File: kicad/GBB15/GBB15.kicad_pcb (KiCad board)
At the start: 4 copper layers, 67 x 15 mm, 74 parts, among them J1 CAN_IN, J10 USB-C, J2 CAN_OUT, J3 MA_THERM, J4 MB_THERM, J5 MA, J6 MB, J7 ENDSTOP1, J8 ENDSTOP2, SW1 BOOT, SW2 RESET, U1 TMC2209-LA-T, U2 STM32G0B1CEU6, U3 TMC2209-LA-T, U4 MAX3051EKA+T, U5 NCP730BMT330TBG, Y1 Crystal_GND24

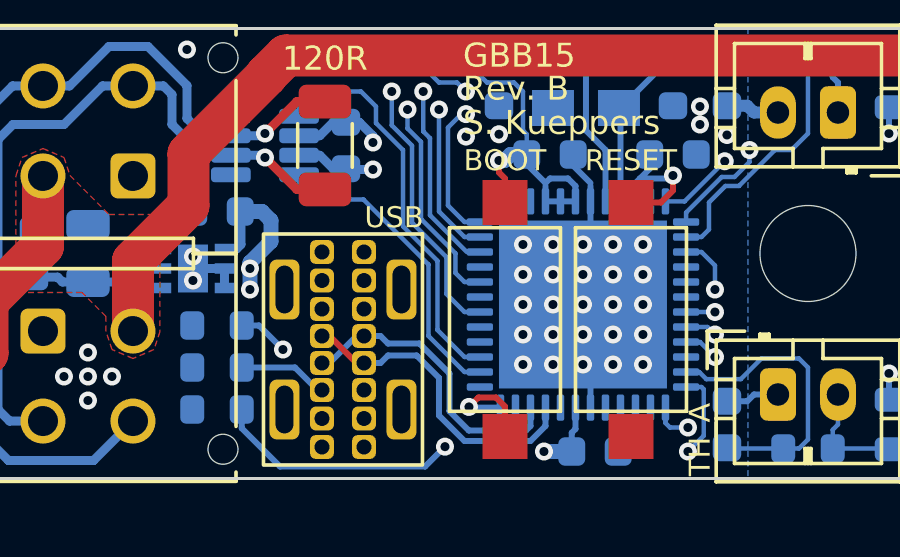
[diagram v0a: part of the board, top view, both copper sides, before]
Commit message: Added additional debug pads for SWD
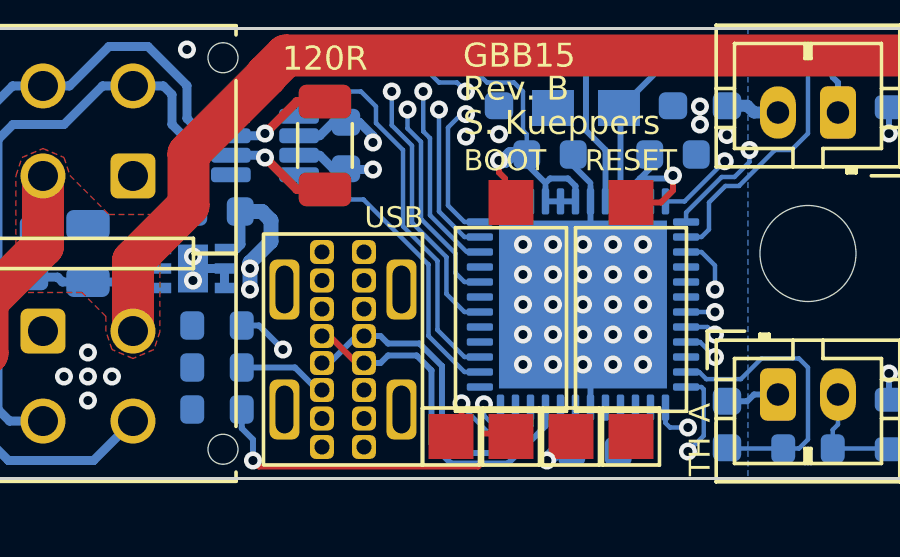
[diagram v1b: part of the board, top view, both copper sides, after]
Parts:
- added TP1: TestPoint, TestPoint:TestPoint_Pad_1.5x1.5mm, F.Cu at (153.6, 98.1)
- added TP2: TestPoint, TestPoint:TestPoint_Pad_1.5x1.5mm, F.Cu at (149.6, 98.1)
- moved SW1 0.20 mm to (151.6, 94.2)
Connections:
- U2 pad 35: unconnected-(U2-Pad35) -> /SWDIO
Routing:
- net /SWDIO: track 0.00 -> 4.25 mm, vias 0 -> 1
- net /USB_DP: track 10.0 -> 11.4 mm
- net /USB_DM: track 10.7 -> 12.0 mm
- net /BOOT0: track 13.2 -> 14.0 mm
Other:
- board text added: "+3V3"
- board text added: "SWCLK"
- board text added: "SWD"
- board text added: "SWDIO"

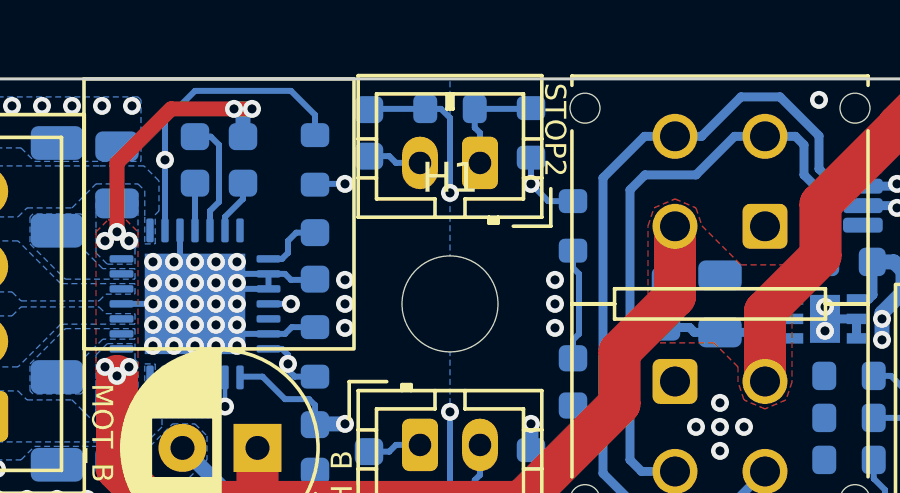
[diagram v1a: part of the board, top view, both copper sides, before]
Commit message: Increased connection width to MicroFit GND pads
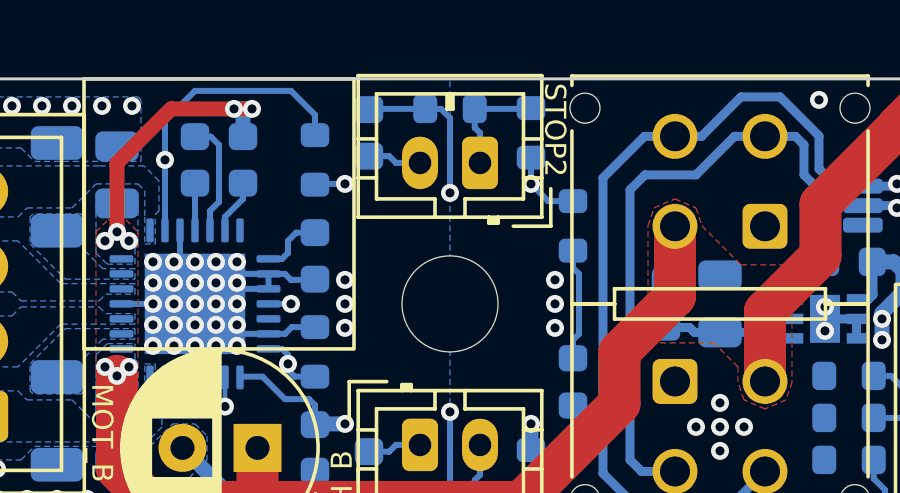
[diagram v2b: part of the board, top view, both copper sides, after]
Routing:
- net GND: track 80.4 -> 90.1 mm
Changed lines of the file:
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@@
     (property "Sheetname" "")
     (attr exclude_from_pos_files)
-    (fp_text reference "H1" (at 0 -4.2) (layer "F.SilkS")
+    (fp_text reference "H1" (at 0 -4.2) (layer "F.SilkS") hide
       (effects (font (size 1 1) (thickness 0.15)))
     )
@@
       (effects (font (size 1 1) (thickness 0.15)))
     )
-    (fp_text value "RESET" (at 4.3 0.3 180) (layer "F.Fab")
+    (fp_text value "RESET" (at 6.5 0.4 180) (layer "F.Fab")
       (effects (font (size 1 1) (thickness 0.15)))
     )
@@
       (effects (font (size 1 1) (thickness 0.15)))
     )
-    (fp_text user "${REFERENCE}" (at 0 -1.65) (layer "F.Fab")
+    (fp_text user "${REFERENCE}" (at 0 -1.65) (layer "F.Fab") hide
       (effects (font (size 1 1) (thickness 0.15)))
     )
@@
       (effects (font (size 1 1) (thickness 0.15)))
     )
-    (fp_text value "USB-C" (at 5.5 0 unlocked) (layer "F.Fab")
+    (fp_text value "USB-C" (at 5.5 0.2 unlocked) (layer "F.Fab")
       (effects (font (size 1 1) (thickness 0.15)))
     )
@@
       (effects (font (size 1 1) (thickness 0.15)))
     )
-    (fp_text user "${REFERENCE}" (at 0 -1.65) (layer "F.Fab")
+    (fp_text user "${REFERENCE}" (at 0 -1.65) (layer "F.Fab") hide
       (effects (font (size 1 1) (thickness 0.15)))
     )
@@
       (effects (font (size 1 1) (thickness 0.15)))
     )
-    (fp_text value "BOOT" (at -4.3 -0.5) (layer "F.Fab")
+    (fp_text value "BOOT" (at -6.5 -0.8) (layer "F.Fab")
       (effects (font (size 1 1) (thickness 0.15)))
     )
@@
       (effects (font (size 1 1) (thickness 0.15)))
     )
-    (fp_text value "MA_THERM" (at 1 4) (layer "F.Fab")
+    (fp_text value "MA_THERM" (at 1.2 4) (layer "F.Fab")
       (effects (font (size 1 1) (thickness 0.15)))
     )
@@
     (fp_line (start 0.8 0.735) (end -1.485 0.735) (layer "B.SilkS") (width 0.12))
     (fp_line (start 1.48 0.73) (end 1.48 -0.73) (layer "B.CrtYd") (width 0.05))
+    (fp_line (start 1.48 -0.73) (end -1.48 -0.73) (layer "B.CrtYd") (width 0.05))
     (fp_line (start -1.48 0.73) (end 1.48 0.73) (layer "B.CrtYd") (width 0.05))
     (fp_line (start -1.48 -0.73) (end -1.48 0.73) (layer "B.CrtYd") (width 0.05))
-    (fp_line (start 1.48 -0.73) (end -1.48 -0.73) (layer "B.CrtYd") (width 0.05))
-    (fp_line (start 0.8 -0.4) (end 0.8 0.4) (layer "B.Fab") (width 0.1))
     (fp_line (start 0.8 0.4) (end -0.5 0.4) (layer "B.Fab") (width 0.1))
-    (fp_line (start -0.8 0.1) (end -0.8 -0.4) (layer "B.Fab") (width 0.1))
     (fp_line (start -0.8 -0.4) (end 0.8 -0.4) (layer "B.Fab") (width 0.1))
     (fp_line (start -0.5 0.4) (end -0.8 0.1) (layer "B.Fab") (width 0.1))
+    (fp_line (start -0.8 0.1) (end -0.8 -0.4) (layer "B.Fab") (width 0.1))
+    (fp_line (start 0.8 -0.4) (end 0.8 0.4) (layer "B.Fab") (width 0.1))
     (pad "1" smd roundrect (at -0.7875 0 90) (size 0.875 0.95) (layers "B.Cu" "B.Paste" "B.Mask") (roundrect_rratio 0.25)
       (net 15 "GND") (pinfunction "K") (pintype "passive"))
@@
   (gr_line (start 137.5 103) (end 137.5 110) (layer "Dwgs.User") (width 0.15))
   (gr_line (start 107 87) (end 101 87) (layer "Dwgs.User") (width 0.15))
-  (gr_line (start 152.6 103) (end 152.6 109) (layer "Dwgs.User") (width 0.15))
+  (gr_line (start 152.6 104) (end 152.6 110) (layer "Dwgs.User") (width 0.15))
   (gr_line (start 183 97) (end 189 97) (layer "Dwgs.User") (width 0.15))
   (gr_line (start 101 87) (end 101 97) (layer "Dwgs.User") (width 0.15))
   (gr_line (start 101 89.5) (end 107 89.5) (layer "Dwgs.User") (width 0.15))
-  (gr_rect (start 148.4 103) (end 156.7 109) (layer "Dwgs.User") (width 0.15) (fill none))
+  (gr_rect (start 148.4 104) (end 156.7 110) (layer "Dwgs.User") (width 0.15) (fill none))
   (gr_line (start 189 89.5) (end 189 87) (layer "Dwgs.User") (width 0.15))
   (gr_line (start 107 89.5) (end 107 87) (layer "Dwgs.User") (width 0.15))
@@
   (gr_line (start 189 87) (end 183 87) (layer "Dwgs.User") (width 0.15))
   (gr_line (start 189 92) (end 183 92) (layer "Dwgs.User") (width 0.15))
-  (gr_line (start 150.5 103) (end 150.5 109) (layer "Dwgs.User") (width 0.15))
+  (gr_line (start 150.5 104) (end 150.5 110) (layer "Dwgs.User") (width 0.15))
   (gr_line (start 189 97) (end 189 89.5) (layer "Dwgs.User") (width 0.15))
   (gr_line (start 189 94.5) (end 183 94.5) (layer "Dwgs.User") (width 0.15))
@@
   (gr_line (start 107 97) (end 107 89.5) (layer "Dwgs.User") (width 0.15))
   (gr_line (start 137.5 74) (end 137.5 81) (layer "Dwgs.User") (width 0.15))
-  (gr_line (start 154.7 103) (end 154.7 109) (layer "Dwgs.User") (width 0.15))
+  (gr_line (start 154.7 104) (end 154.7 110) (layer "Dwgs.User") (width 0.15))
   (gr_line (start 183 89.5) (end 189 89.5) (layer "Dwgs.User") (width 0.15))
   (gr_line (start 107 94.5) (end 101 94.5) (layer "Dwgs.User") (width 0.15))
@@
     (effects (font (size 1 1) (thickness 0.15)))
   )
-  (gr_text "SWCLK\n" (at 151.6 105.7 90) (layer "Dwgs.User")
+  (gr_text "SWCLK\n" (at 151.6 106.7 90) (layer "Dwgs.User")
     (effects (font (size 1 1) (thickness 0.15)))
   )
@@
     (effects (font (size 1 1) (thickness 0.15)))
   )
-  (gr_text "+3V3" (at 153.7 105.7 90) (layer "Dwgs.User")
+  (gr_text "+3V3" (at 153.7 106.7 90) (layer "Dwgs.User")
     (effects (font (size 1 1) (thickness 0.15)))
   )
@@
     (effects (font (size 1 1) (thickness 0.15)))
   )
-  (gr_text "SWD" (at 152.5 100.7) (layer "Dwgs.User")
+  (gr_text "SWD" (at 152.6 103.2) (layer "Dwgs.User")
     (effects (font (size 1 1) (thickness 0.15)))
   )
@@
     (effects (font (size 1 1) (thickness 0.15)))
   )
-  (gr_text "SWDIO\n" (at 149.5 105.7 90) (layer "Dwgs.User")
+  (gr_text "SWDIO\n" (at 149.5 106.7 90) (layer "Dwgs.User")
     (effects (font (size 1 1) (thickness 0.15)))
   )
@@
     (effects (font (size 1 1) (thickness 0.15)))
   )
-  (gr_text "GND" (at 155.8 105.7 90) (layer "Dwgs.User")
+  (gr_text "GND" (at 155.8 106.7 90) (layer "Dwgs.User")
     (effects (font (size 1 1) (thickness 0.15)))
   )
@@
   (via (at 132 91.2) (size 0.6) (drill 0.3) (layers "F.Cu" "B.Cu") (net 15))
   (via (at 118.6 90.6) (size 0.6) (drill 0.3) (layers "F.Cu" "B.Cu") (net 15))
+  (segment (start 139 89.4) (end 137.785 89.4) (width 0.8) (layer "In1.Cu") (net 15))
+  (segment (start 139 89.4) (end 140.215 89.4) (width 0.8) (layer "In1.Cu") (net 15))
   (segment (start 145.3 98.45) (end 146.05 98.45) (width 0.2) (layer "In1.Cu") (net 15))
+  (segment (start 139 89.4) (end 139 90.615) (width 0.8) (layer "In1.Cu") (net 15))
+  (segment (start 139 89.415) (end 139 88.2) (width 0.8) (layer "In1.Cu") (net 15))
+  (segment (start 136 94.6) (end 136 95.815) (width 0.8) (layer "In1.Cu") (net 15))
+  (segment (start 136 94.6) (end 137.215 94.6) (width 0.8) (layer "In1.Cu") (net 15))
+  (segment (start 136 94.6) (end 134.785 94.6) (width 0.8) (layer "In1.Cu") (net 15))
   (segment (start 146 92) (end 146.05 91.95) (width 0.2) (layer "In1.Cu") (net 15))
+  (segment (start 136 94.615) (end 136 93.4) (width 0.8) (layer "In1.Cu") (net 15))
   (segment (start 146 98.4) (end 146 92) (width 0.2) (layer "In1.Cu") (net 15))
   (segment (start 146.05 98.45) (end 146.7 98.45) (width 0.2) (layer "In1.Cu") (net 15))

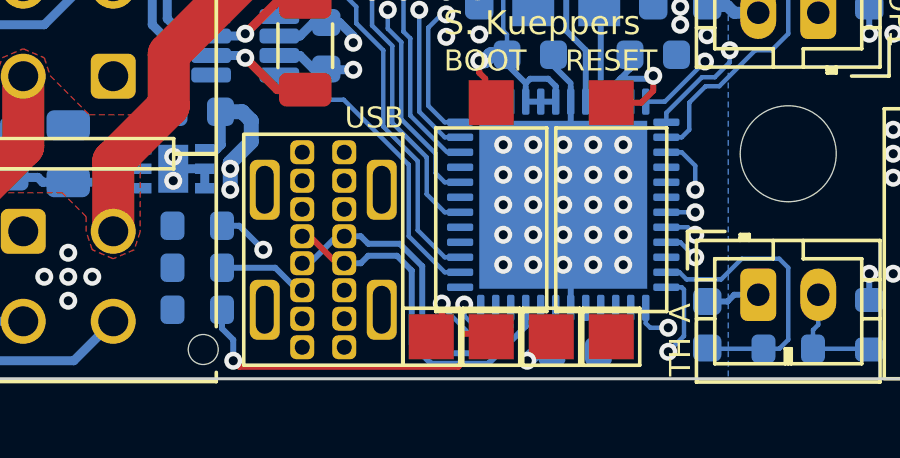
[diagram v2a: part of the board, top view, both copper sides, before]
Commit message: Minor trace changes
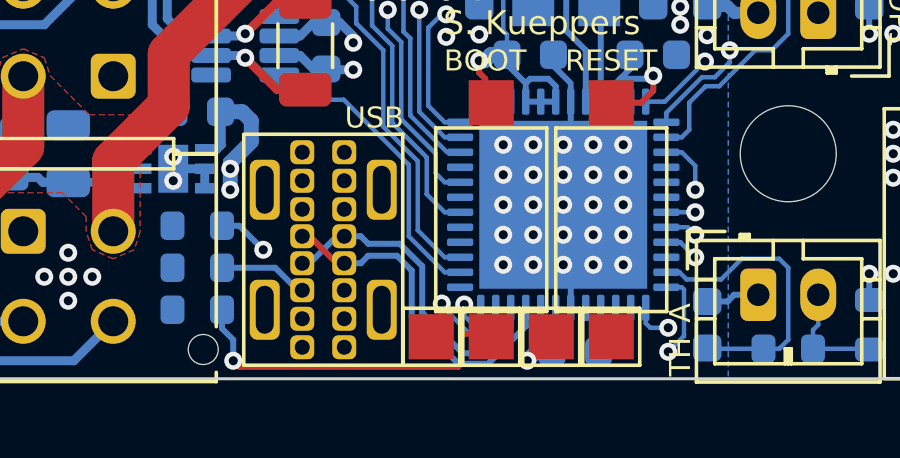
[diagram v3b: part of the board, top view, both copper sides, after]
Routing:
- net /USB_DP: track 11.4 -> 10.8 mm
- net /USB_DM: track 12.0 -> 11.5 mm
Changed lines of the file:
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@@
   (segment (start 146.7 95.65) (end 146.45 95.65) (width 0.2) (layer "F.Cu") (net 13))
   (segment (start 145.55 94.75) (end 145.3 94.75) (width 0.2) (layer "F.Cu") (net 13))
+  (segment (start 147.25 95.65) (end 146.7 95.65) (width 0.2) (layer "B.Cu") (net 13))
+  (segment (start 151.5 99) (end 150.505703 98.999999) (width 0.2) (layer "B.Cu") (net 13))
+  (segment (start 148.455704 95.4) (end 147.5 95.4) (width 0.2) (layer "B.Cu") (net 13))
   (segment (start 152.75 97.1375) (end 152.75 97.75) (width 0.2) (layer "B.Cu") (net 13))
+  (segment (start 148.95048 95.894776) (end 148.455704 95.4) (width 0.2) (layer "B.Cu") (net 13))
+  (segment (start 148.95048 97.444776) (end 148.95048 95.894776) (width 0.2) (layer "B.Cu") (net 13))
+  (segment (start 152.75 97.75) (end 151.5 99) (width 0.2) (layer "B.Cu") (net 13))
   (segment (start 147.5 95.4) (end 147.25 95.65) (width 0.2) (layer "B.Cu") (net 13))
-  (segment (start 148.95048 95.894776) (end 148.455704 95.4) (width 0.2) (layer "B.Cu") (net 13))
-  (segment (start 152.75 97.75) (end 151.5 99) (width 0.2) (layer "B.Cu") (net 13))
-  (segment (start 151.5 99) (end 149.599999 98.999999) (width 0.2) (layer "B.Cu") (net 13))
-  (segment (start 148.95048 98.350479) (end 148.95048 95.894776) (width 0.2) (layer "B.Cu") (net 13))
-  (segment (start 149.599999 98.999999) (end 148.95048 98.350479) (width 0.2) (layer "B.Cu") (net 13))
-  (segment (start 148.455704 95.4) (end 147.5 95.4) (width 0.2) (layer "B.Cu") (net 13))
-  (segment (start 147.25 95.65) (end 146.7 95.65) (width 0.2) (layer "B.Cu") (net 13))
-  (segment (start 149.744776 98.65048) (end 149.3 98.205704) (width 0.2) (layer "B.Cu") (net 14))
+  (segment (start 150.505703 98.999999) (end 148.95048 97.444776) (width 0.2) (layer "B.Cu") (net 13))
+  (segment (start 149.3 95.75) (end 148.55 95) (width 0.2) (layer "B.Cu") (net 14))
   (segment (start 152.25 97.1375) (end 152.25 97.75) (width 0.2) (layer "B.Cu") (net 14))
-  (segment (start 152.25 97.75) (end 151.34952 98.65048) (width 0.2) (layer "B.Cu") (net 14))
   (segment (start 147.5 95) (end 147.25 94.75) (width 0.2) (layer "B.Cu") (net 14))
-  (segment (start 148.55 95) (end 147.5 95) (width 0.2) (layer "B.Cu") (net 14))
-  (segment (start 149.3 98.205704) (end 149.3 95.75) (width 0.2) (layer "B.Cu") (net 14))
-  (segment (start 149.3 95.75) (end 148.55 95) (width 0.2) (layer "B.Cu") (net 14))
   (segment (start 146.7 94.75) (end 146.45 94.75) (width 0.2) (layer "B.Cu") (net 14))
   (segment (start 147.25 94.75) (end 146.7 94.75) (width 0.2) (layer "B.Cu") (net 14))
+  (segment (start 152.25 97.75) (end 151.34952 98.65048) (width 0.2) (layer "B.Cu") (net 14))
   (segment (start 145.55 95.65) (end 145.3 95.65) (width 0.2) (layer "B.Cu") (net 14))
-  (segment (start 151.34952 98.65048) (end 149.744776 98.65048) (width 0.2) (layer "B.Cu") (net 14))
+  (segment (start 149.3 97.3) (end 149.3 95.75) (width 0.2) (layer "B.Cu") (net 14))
+  (segment (start 151.34952 98.65048) (end 150.65048 98.65048) (width 0.2) (layer "B.Cu") (net 14))
+  (segment (start 148.55 95) (end 147.5 95) (width 0.2) (layer "B.Cu") (net 14))
   (segment (start 146.45 94.75) (end 145.55 95.65) (width 0.2) (layer "B.Cu") (net 14))
+  (segment (start 150.65048 98.65048) (end 149.3 97.3) (width 0.2) (layer "B.Cu") (net 14))
   (via (at 114.9 85.4) (size 0.6) (drill 0.3) (layers "F.Cu" "B.Cu") (free) (net 15))
   (via (at 155 94.7) (size 0.6) (drill 0.3) (layers "F.Cu" "B.Cu") (net 15))
